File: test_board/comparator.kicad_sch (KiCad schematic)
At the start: 9 parts, among them U1 TLV3601DCKR

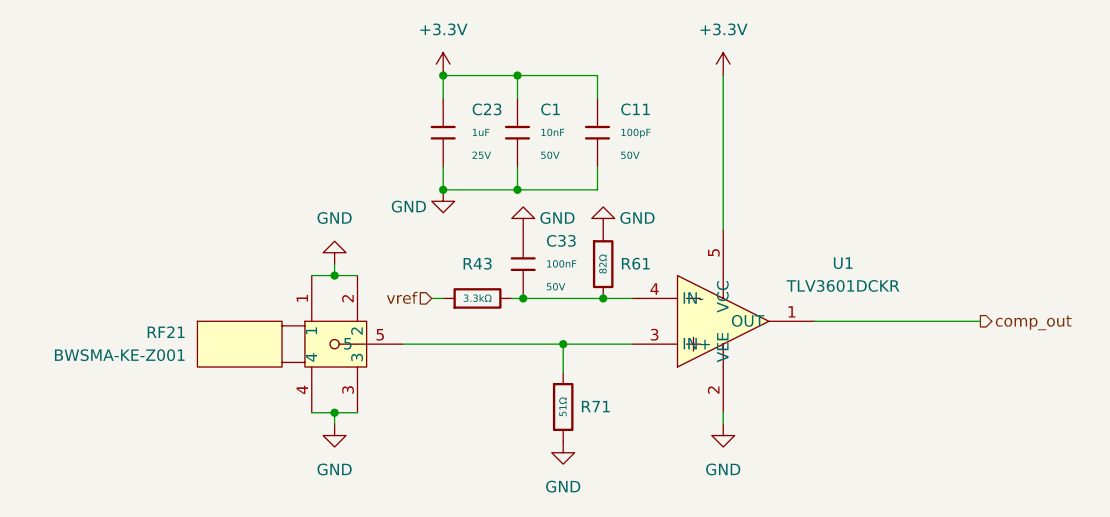
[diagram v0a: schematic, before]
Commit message: added decoupling caps to regulator and changed comparator termination resistor to 49.9 ohm
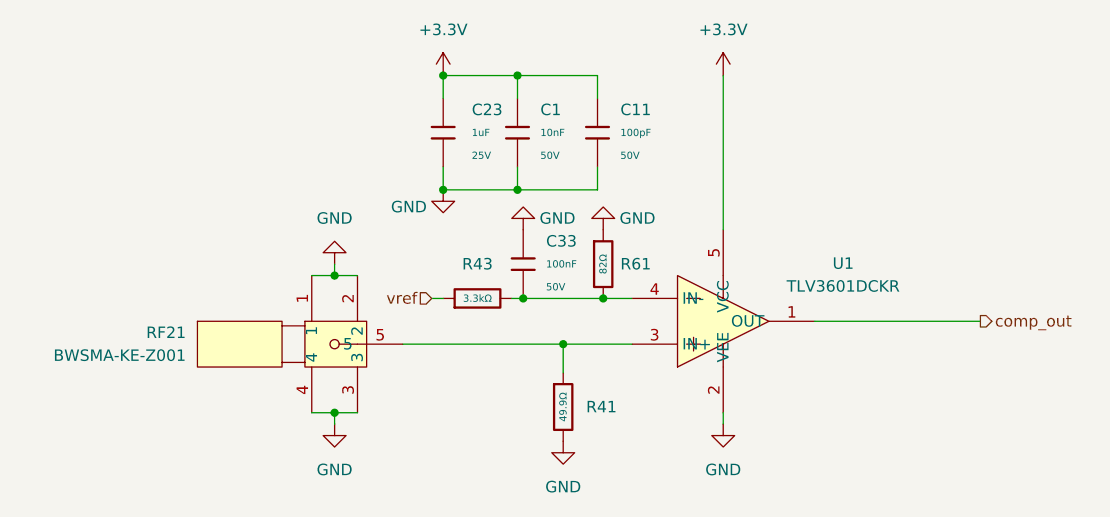
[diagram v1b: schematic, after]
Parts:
- removed R71: 51Ω, PCM_JLCPCB:R_0402, symbol PCM_JLCPCB-Resistors:0402,51Ω
- added R41: 49.9Ω, PCM_JLCPCB:R_0402, symbol PCM_JLCPCB-Resistors:0402,49.9Ω
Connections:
- net GND: now also R41.2
- net at RF21.5, U1.3 (IN+): now also R41.1

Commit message: added 0 ohm resistor
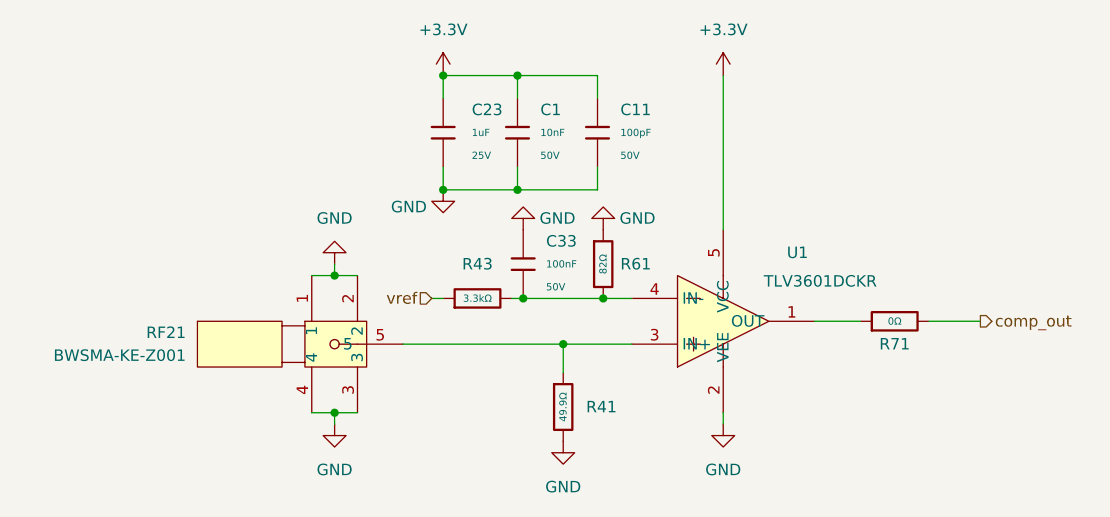
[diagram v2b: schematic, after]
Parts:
- added R71: 0Ω, PCM_JLCPCB:R_0402, symbol PCM_JLCPCB-Resistors:0402,0Ω
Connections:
- net comp_out: now also R71.2; no longer U1.1 (OUT)
- new net: R71.1, U1.1 (OUT)
